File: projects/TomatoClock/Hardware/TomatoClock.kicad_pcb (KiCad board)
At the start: 2 copper layers, 4 parts, among them U1 ATmega328P-PU, Y1 16MHz

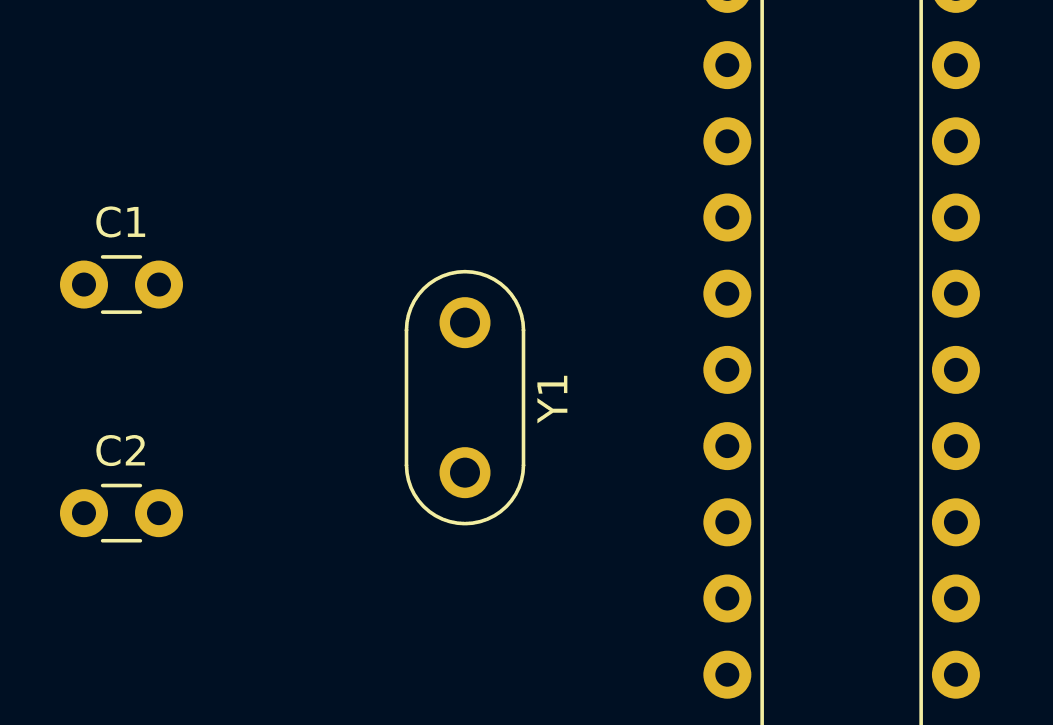
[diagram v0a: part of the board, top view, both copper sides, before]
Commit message: TomatoClock: Update hardware schematics
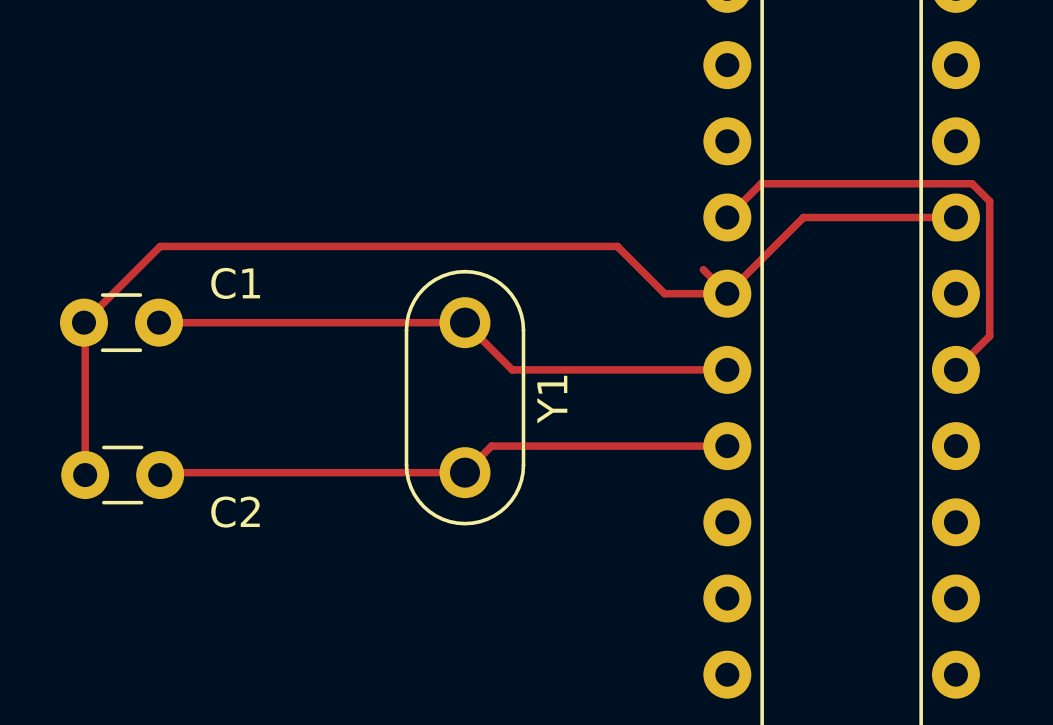
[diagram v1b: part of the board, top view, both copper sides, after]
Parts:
- moved C2 2.84 mm to (63.5, 167.6), turned to 180 degrees
- moved C1 1.27 mm to (61.0, 162.6)
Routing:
- net GND: track 0.00 -> 38.1 mm
- net Net-(C1-Pad2): track 0.00 -> 19.6 mm
- net Net-(C2-Pad1): track 0.00 -> 19.3 mm
- net +3V3: track 0.00 -> 15.5 mm
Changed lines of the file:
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@@
     (thickness 1.6)
     (drawings 0)
-    (tracks 0)
+    (tracks 22)
     (zones 0)
     (modules 4)
@@
     (pad_to_mask_clearance 0)
     (aux_axis_origin 0 0)
-    (visible_elements FFFFFF7F)
+    (visible_elements 7FFFFFFF)
     (pcbplotparams
       (layerselection 0x010fc_ffffffff)
@@
   )
   (module Capacitor_THT:C_Disc_D3.0mm_W1.6mm_P2.50mm (layer F.Cu)
-    (at 60.96 161.29)
+    (at 63.5 167.64 180)
     (descr "C, Disc series, Radial, pin pitch=2.50mm, , diameter*width=3.0*1.6mm^2, Capacitor, http://www.vishay.com/docs/45233/krseries.pdf")
     (tags "C Disc series Radial pin pitch 2.50mm  diameter 3.0mm width 1.6mm Capacitor")
-    (fp_text reference C1 (at 1.25 -2.05) (layer F.SilkS)
-      (effects (font (size 1 1) (thickness 0.15)))
-    )
-    (fp_text value 22pF (at 1.25 2.05) (layer F.Fab)
+    (fp_text reference C2 (at -2.54 -1.27) (layer F.SilkS)
+      (effects (font (size 1 1) (thickness 0.15)))
+    )
+    (fp_text value 22pF (at -3.175 1.27) (layer F.Fab)
       (effects (font (size 1 1) (thickness 0.15)))
     )
@@
       (effects (font (size 0.6 0.6) (thickness 0.09)))
     )
-    (pad 1 thru_hole circle (at 0 0) (size 1.6 1.6) (drill 0.8) (layers *.Cu *.Mask)
+    (pad 2 thru_hole circle (at 2.5 0 180) (size 1.6 1.6) (drill 0.8) (layers *.Cu *.Mask)
       (net 1 GND))
-    (pad 2 thru_hole circle (at 2.5 0) (size 1.6 1.6) (drill 0.8) (layers *.Cu *.Mask)
-      (net 2 "Net-(C1-Pad2)"))
+    (pad 1 thru_hole circle (at 0 0 180) (size 1.6 1.6) (drill 0.8) (layers *.Cu *.Mask)
+      (net 3 "Net-(C2-Pad1)"))
     (model ${KISYS3DMOD}/Capacitor_THT.3dshapes/C_Disc_D3.0mm_W1.6mm_P2.50mm.wrl
       (at (xyz 0 0 0))
@@
   )
   (module Capacitor_THT:C_Disc_D3.0mm_W1.6mm_P2.50mm (layer F.Cu)
-    (at 60.96 168.91)
+    (at 60.96 162.56)
     (descr "C, Disc series, Radial, pin pitch=2.50mm, , diameter*width=3.0*1.6mm^2, Capacitor, http://www.vishay.com/docs/45233/krseries.pdf")
     (tags "C Disc series Radial pin pitch 2.50mm  diameter 3.0mm width 1.6mm Capacitor")
-    (fp_text reference C2 (at 1.25 -2.05) (layer F.SilkS)
-      (effects (font (size 1 1) (thickness 0.15)))
-    )
-    (fp_text value 22pF (at 1.25 2.05) (layer F.Fab)
-      (effects (font (size 1 1) (thickness 0.15)))
-    )
-    (fp_text user %R (at 1.25 0) (layer F.Fab)
-      (effects (font (size 0.6 0.6) (thickness 0.09)))
+    (fp_text reference C1 (at 5.08 -1.27) (layer F.SilkS)
+      (effects (font (size 1 1) (thickness 0.15)))
+    )
+    (fp_text value 22pF (at 5.715 1.27) (layer F.Fab)
+      (effects (font (size 1 1) (thickness 0.15)))
     )
     (fp_line (start -0.25 -0.8) (end -0.25 0.8) (layer F.Fab) (width 0.1))
@@
     (fp_line (start 3.55 1.05) (end 3.55 -1.05) (layer F.CrtYd) (width 0.05))
     (fp_line (start 3.55 -1.05) (end -1.05 -1.05) (layer F.CrtYd) (width 0.05))
+    (fp_text user %R (at 1.25 0) (layer F.Fab)
+      (effects (font (size 0.6 0.6) (thickness 0.09)))
+    )
+    (pad 1 thru_hole circle (at 0 0) (size 1.6 1.6) (drill 0.8) (layers *.Cu *.Mask)
+      (net 1 GND))
     (pad 2 thru_hole circle (at 2.5 0) (size 1.6 1.6) (drill 0.8) (layers *.Cu *.Mask)
-      (net 1 GND))
-    (pad 1 thru_hole circle (at 0 0) (size 1.6 1.6) (drill 0.8) (layers *.Cu *.Mask)
-      (net 3 "Net-(C2-Pad1)"))
+      (net 2 "Net-(C1-Pad2)"))
     (model ${KISYS3DMOD}/Capacitor_THT.3dshapes/C_Disc_D3.0mm_W1.6mm_P2.50mm.wrl
       (at (xyz 0 0 0))
@@
       (effects (font (size 1 1) (thickness 0.15)))
     )
+    (fp_line (start 1.635 -1.27) (end 6.985 -1.27) (layer F.Fab) (width 0.1))
+    (fp_line (start 6.985 -1.27) (end 6.985 34.29) (layer F.Fab) (width 0.1))
+    (fp_line (start 6.985 34.29) (end 0.635 34.29) (layer F.Fab) (width 0.1))
+    (fp_line (start 0.635 34.29) (end 0.635 -0.27) (layer F.Fab) (width 0.1))
+    (fp_line (start 0.635 -0.27) (end 1.635 -1.27) (layer F.Fab) (width 0.1))
+    (fp_line (start 2.81 -1.33) (end 1.16 -1.33) (layer F.SilkS) (width 0.12))
+    (fp_line (start 1.16 -1.33) (end 1.16 34.35) (layer F.SilkS) (width 0.12))
+    (fp_line (start 1.16 34.35) (end 6.46 34.35) (layer F.SilkS) (width 0.12))
+    (fp_line (start 6.46 34.35) (end 6.46 -1.33) (layer F.SilkS) (width 0.12))
+    (fp_line (start 6.46 -1.33) (end 4.81 -1.33) (layer F.SilkS) (width 0.12))
+    (fp_line (start -1.1 -1.55) (end -1.1 34.55) (layer F.CrtYd) (width 0.05))
+    (fp_line (start -1.1 34.55) (end 8.7 34.55) (layer F.CrtYd) (width 0.05))
+    (fp_line (start 8.7 34.55) (end 8.7 -1.55) (layer F.CrtYd) (width 0.05))
     (fp_line (start 8.7 -1.55) (end -1.1 -1.55) (layer F.CrtYd) (width 0.05))
-    (fp_line (start 8.7 34.55) (end 8.7 -1.55) (layer F.CrtYd) (width 0.05))
-    (fp_line (start -1.1 34.55) (end 8.7 34.55) (layer F.CrtYd) (width 0.05))
-    (fp_line (start -1.1 -1.55) (end -1.1 34.55) (layer F.CrtYd) (width 0.05))
-    (fp_line (start 6.46 -1.33) (end 4.81 -1.33) (layer F.SilkS) (width 0.12))
-    (fp_line (start 6.46 34.35) (end 6.46 -1.33) (layer F.SilkS) (width 0.12))
-    (fp_line (start 1.16 34.35) (end 6.46 34.35) (layer F.SilkS) (width 0.12))
-    (fp_line (start 1.16 -1.33) (end 1.16 34.35) (layer F.SilkS) (width 0.12))
-    (fp_line (start 2.81 -1.33) (end 1.16 -1.33) (layer F.SilkS) (width 0.12))
-    (fp_line (start 0.635 -0.27) (end 1.635 -1.27) (layer F.Fab) (width 0.1))
-    (fp_line (start 0.635 34.29) (end 0.635 -0.27) (layer F.Fab) (width 0.1))
-    (fp_line (start 6.985 34.29) (end 0.635 34.29) (layer F.Fab) (width 0.1))
-    (fp_line (start 6.985 -1.27) (end 6.985 34.29) (layer F.Fab) (width 0.1))
-    (fp_line (start 1.635 -1.27) (end 6.985 -1.27) (layer F.Fab) (width 0.1))
     (fp_arc (start 3.81 -1.33) (end 2.81 -1.33) (angle -180) (layer F.SilkS) (width 0.12))
     (fp_text user %R (at 3.81 16.51) (layer F.Fab)
@@
       (effects (font (size 1 1) (thickness 0.15)))
     )
-    (fp_line (start 7 -2.2) (end -2 -2.2) (layer F.CrtYd) (width 0.05))
-    (fp_line (start 7 2.2) (end 7 -2.2) (layer F.CrtYd) (width 0.05))
-    (fp_line (start -2 2.2) (end 7 2.2) (layer F.CrtYd) (width 0.05))
-    (fp_line (start -2 -2.2) (end -2 2.2) (layer F.CrtYd) (width 0.05))
-    (fp_line (start 0.25 1.95) (end 4.75 1.95) (layer F.SilkS) (width 0.12))
-    (fp_line (start 0.25 -1.95) (end 4.75 -1.95) (layer F.SilkS) (width 0.12))
+    (fp_line (start 0.25 -1.75) (end 4.75 -1.75) (layer F.Fab) (width 0.1))
     (fp_line (start 0.25 1.75) (end 4.75 1.75) (layer F.Fab) (width 0.1))
     (fp_line (start 0.25 -1.75) (end 4.75 -1.75) (layer F.Fab) (width 0.1))
     (fp_line (start 0.25 1.75) (end 4.75 1.75) (layer F.Fab) (width 0.1))
-    (fp_line (start 0.25 -1.75) (end 4.75 -1.75) (layer F.Fab) (width 0.1))
+    (fp_line (start 0.25 -1.95) (end 4.75 -1.95) (layer F.SilkS) (width 0.12))
+    (fp_line (start 0.25 1.95) (end 4.75 1.95) (layer F.SilkS) (width 0.12))
+    (fp_line (start -2 -2.2) (end -2 2.2) (layer F.CrtYd) (width 0.05))
+    (fp_line (start -2 2.2) (end 7 2.2) (layer F.CrtYd) (width 0.05))
+    (fp_line (start 7 2.2) (end 7 -2.2) (layer F.CrtYd) (width 0.05))
+    (fp_line (start 7 -2.2) (end -2 -2.2) (layer F.CrtYd) (width 0.05))
     (fp_text user %R (at 2.5 0 90) (layer F.Fab)
       (effects (font (size 1 1) (thickness 0.15)))
@@
     )
   )
+  (segment (start 84.945001 159.055001) (end 82.405001 161.595001) (width 0.25) (layer F.Cu) (net 1))
+  (segment (start 90.025001 159.055001) (end 84.945001 159.055001) (width 0.25) (layer F.Cu) (net 1))
+  (segment (start 82.405001 161.595001) (end 81.605002 160.795002) (width 0.25) (layer F.Cu) (net 1))
+  (segment (start 60.96 167.6) (end 61 167.64) (width 0.25) (layer F.Cu) (net 1))
+  (segment (start 61 162.6) (end 60.96 162.56) (width 0.25) (layer F.Cu) (net 1))
+  (segment (start 61 167.64) (end 61 162.6) (width 0.25) (layer F.Cu) (net 1))
+  (segment (start 60.96 162.56) (end 63.5 160.02) (width 0.25) (layer F.Cu) (net 1))
+  (segment (start 63.5 160.02) (end 78.74 160.02) (width 0.25) (layer F.Cu) (net 1))
+  (segment (start 80.315001 161.595001) (end 82.405001 161.595001) (width 0.25) (layer F.Cu) (net 1))
+  (segment (start 78.74 160.02) (end 80.315001 161.595001) (width 0.25) (layer F.Cu) (net 1))
+  (segment (start 75.235001 164.135001) (end 73.66 162.56) (width 0.25) (layer F.Cu) (net 2))
+  (segment (start 82.405001 164.135001) (end 75.235001 164.135001) (width 0.25) (layer F.Cu) (net 2))
+  (segment (start 73.66 162.56) (end 63.46 162.56) (width 0.25) (layer F.Cu) (net 2))
+  (segment (start 74.544999 166.675001) (end 73.66 167.56) (width 0.25) (layer F.Cu) (net 3))
+  (segment (start 82.405001 166.675001) (end 74.544999 166.675001) (width 0.25) (layer F.Cu) (net 3))
+  (segment (start 63.58 167.56) (end 63.5 167.64) (width 0.25) (layer F.Cu) (net 3))
+  (segment (start 73.66 167.56) (end 63.58 167.56) (width 0.25) (layer F.Cu) (net 3))
+  (segment (start 83.530002 157.93) (end 82.405001 159.055001) (width 0.25) (layer F.Cu) (net 15))
+  (segment (start 90.565002 157.93) (end 83.530002 157.93) (width 0.25) (layer F.Cu) (net 15))
+  (segment (start 91.150002 158.515) (end 90.565002 157.93) (width 0.25) (layer F.Cu) (net 15))
+  (segment (start 91.150002 163.01) (end 91.150002 158.515) (width 0.25) (layer F.Cu) (net 15))
+  (segment (start 90.025001 164.135001) (end 91.150002 163.01) (width 0.25) (layer F.Cu) (net 15))
 )

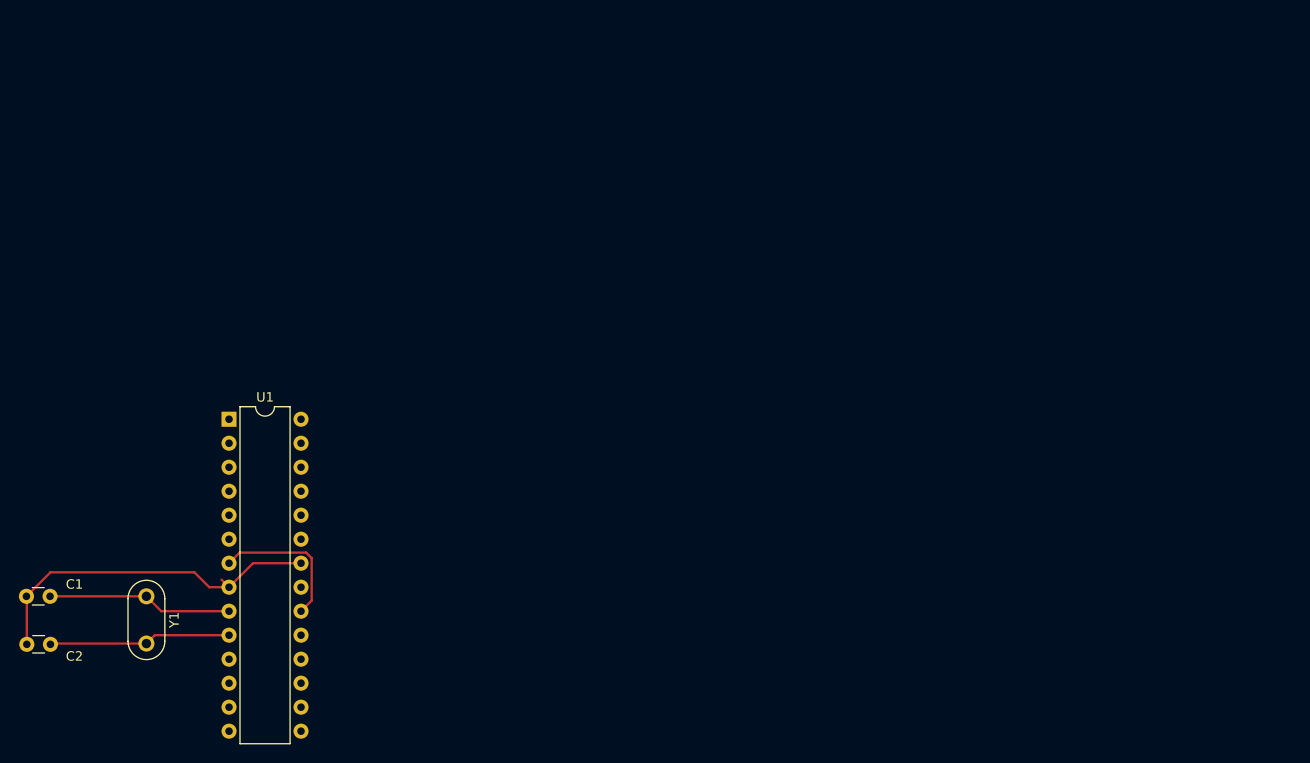
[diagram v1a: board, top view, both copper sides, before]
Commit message: TomatoClock: Update hardware
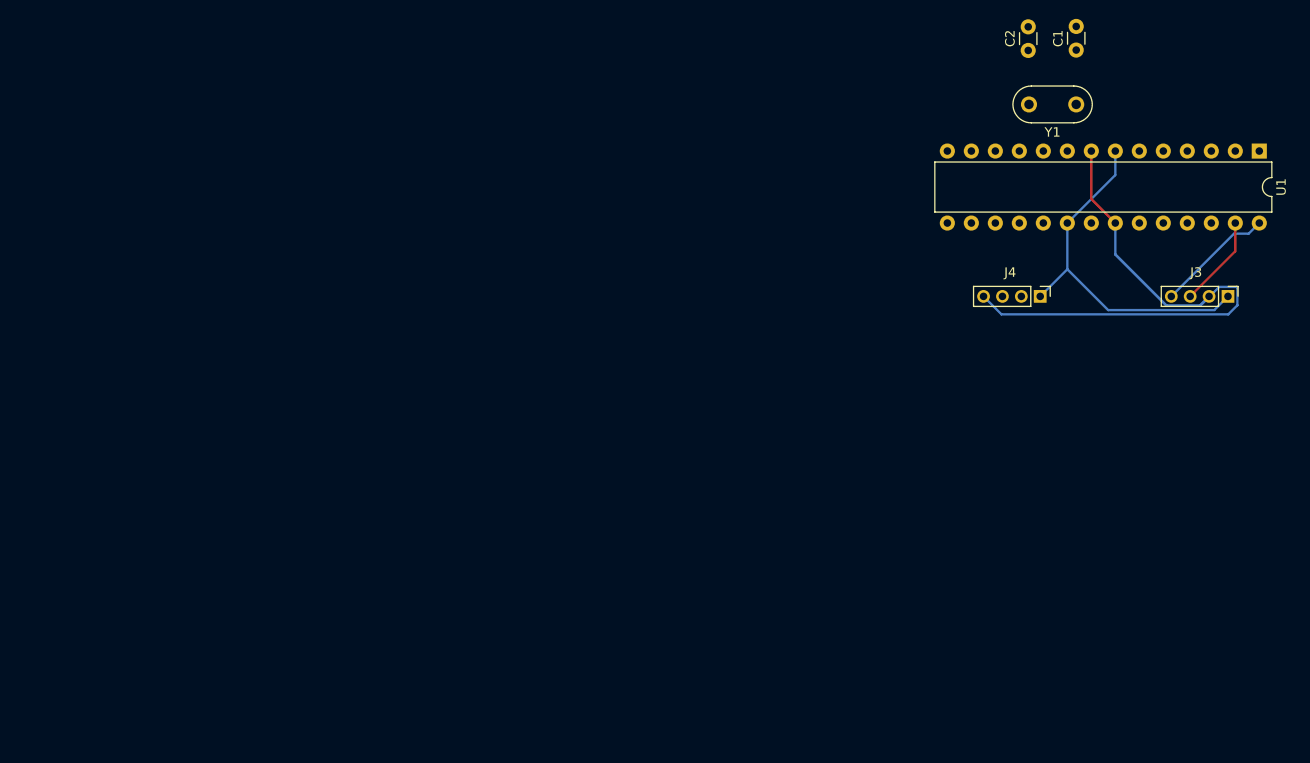
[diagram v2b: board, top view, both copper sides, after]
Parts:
- added J3: Screen, Connector_PinHeader_2.00mm:PinHeader_1x04_P2.00mm_Vertical, F.Cu at (188.2, 130.8)
- added J4: Ultrasonic, Connector_PinHeader_2.00mm:PinHeader_1x04_P2.00mm_Vertical, F.Cu at (168.3, 130.8)
- moved C1 126.4 mm to (172.1, 102.2), turned to 270 degrees
- moved C2 121.1 mm to (167.0, 104.8), turned to 90 degrees
- moved U1 112.7 mm to (191.5, 115.4), turned to 270 degrees
- moved Y1 111.3 mm to (172.1, 110.5), turned to 180 degrees
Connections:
- U1 pad 1: Net-(U1-Pad1) -> (no net)
- U1 pad 11: Net-(U1-Pad11) -> (no net)
- U1 pad 12: Net-(U1-Pad12) -> (no net)
- U1 pad 13: Net-(U1-Pad13) -> (no net)
- U1 pad 14: Net-(U1-Pad14) -> (no net)
- U1 pad 15: Net-(U1-Pad15) -> (no net)
- U1 pad 16: Net-(U1-Pad16) -> (no net)
- U1 pad 17: Net-(U1-Pad17) -> (no net)
- U1 pad 18: Net-(U1-Pad18) -> (no net)
- U1 pad 19: Net-(U1-Pad19) -> (no net)
- U1 pad 2: Net-(U1-Pad2) -> (no net)
- U1 pad 21: Net-(U1-Pad21) -> (no net)
- U1 pad 23: Net-(U1-Pad23) -> (no net)
- U1 pad 24: Net-(U1-Pad24) -> (no net)
- U1 pad 25: Net-(U1-Pad25) -> (no net)
- U1 pad 26: Net-(U1-Pad26) -> (no net)
- U1 pad 27: Net-(U1-Pad27) -> SDA
- U1 pad 28: Net-(U1-Pad28) -> SCL
- U1 pad 3: Net-(U1-Pad3) -> (no net)
- U1 pad 4: Net-(U1-Pad4) -> (no net)
- U1 pad 5: Net-(U1-Pad5) -> (no net)
- U1 pad 6: Net-(U1-Pad6) -> (no net)
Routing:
- net GND: track 38.1 -> 71.8 mm
- net +3V3: track 15.5 -> 38.1 mm
- net Net-(C1-Pad2): track 19.6 -> 0.00 mm
- net Net-(C2-Pad1): track 19.3 -> 0.11 mm
- net SCL: track 0.00 -> 12.5 mm
- net SDA: track 0.00 -> 9.74 mm
